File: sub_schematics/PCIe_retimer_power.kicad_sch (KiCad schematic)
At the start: 40 parts, among them U2 LMQ644A2QRXARQ1

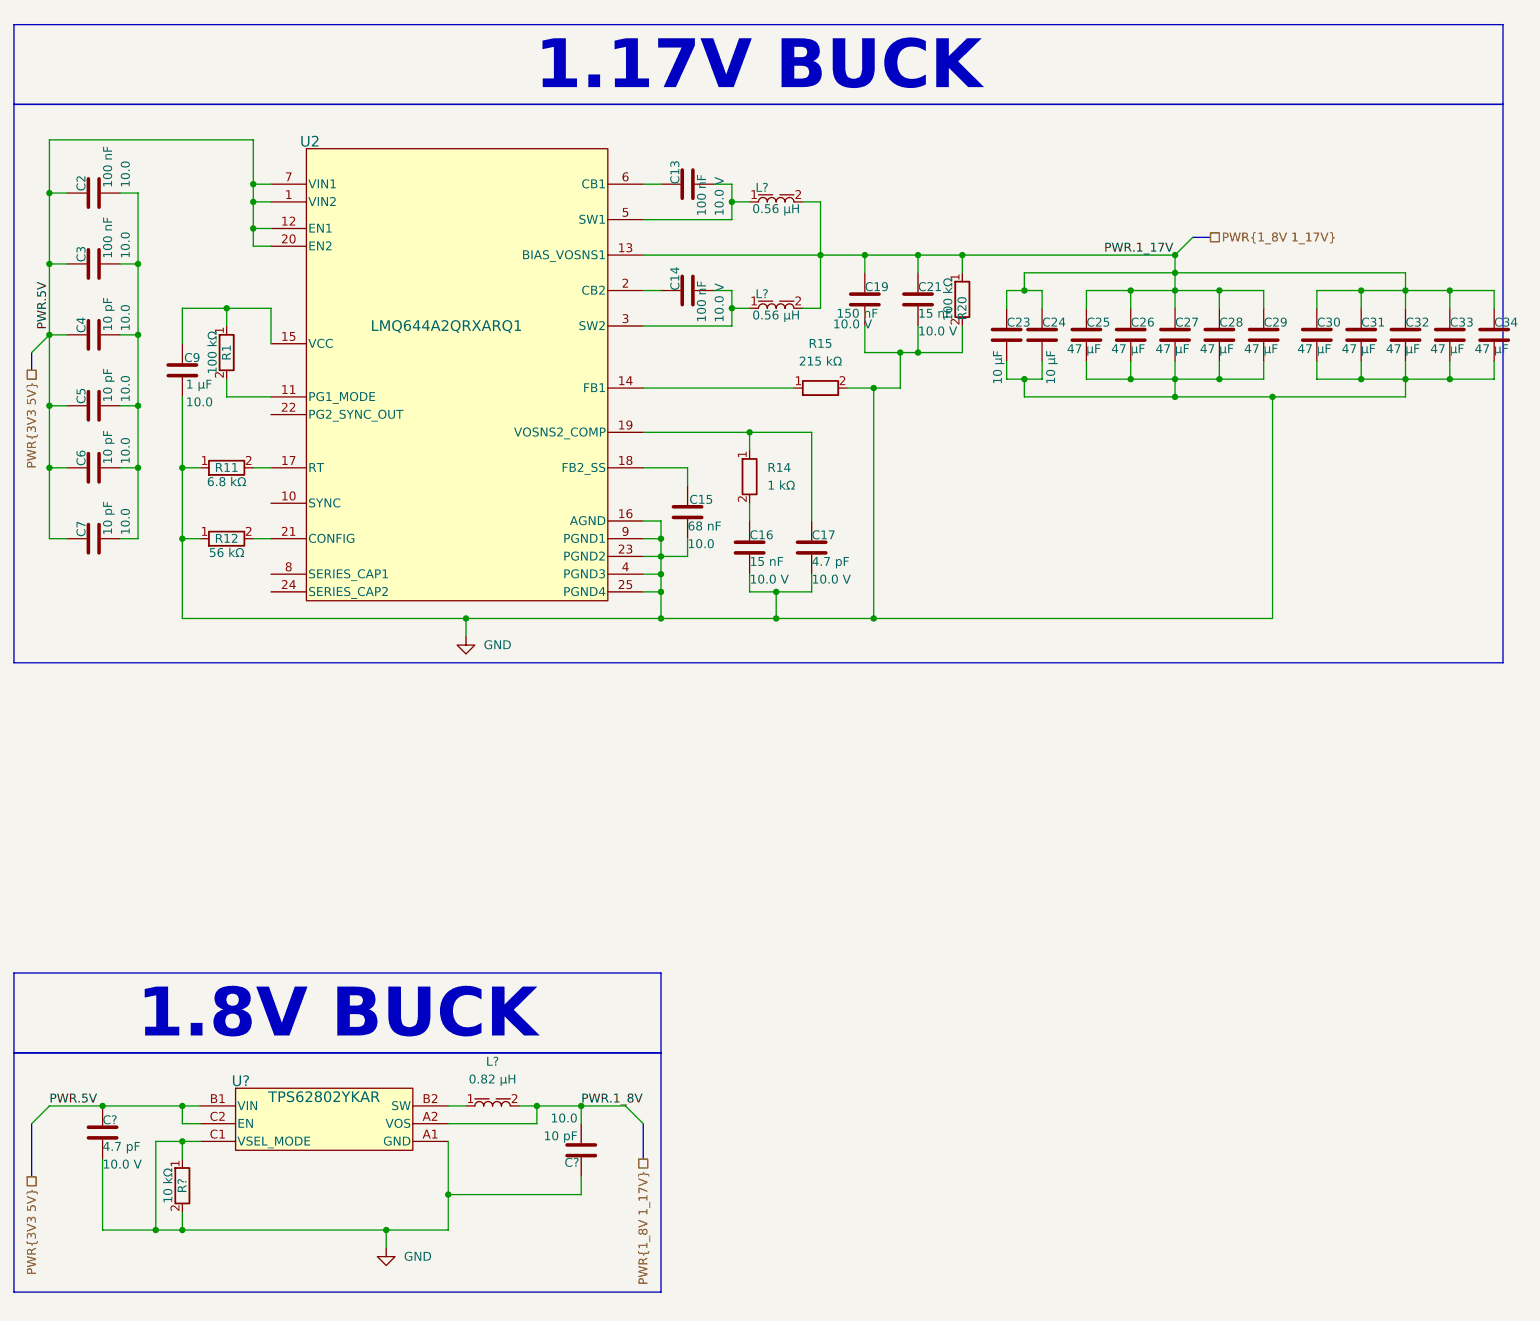
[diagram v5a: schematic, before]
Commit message: Buck closer to recommended value
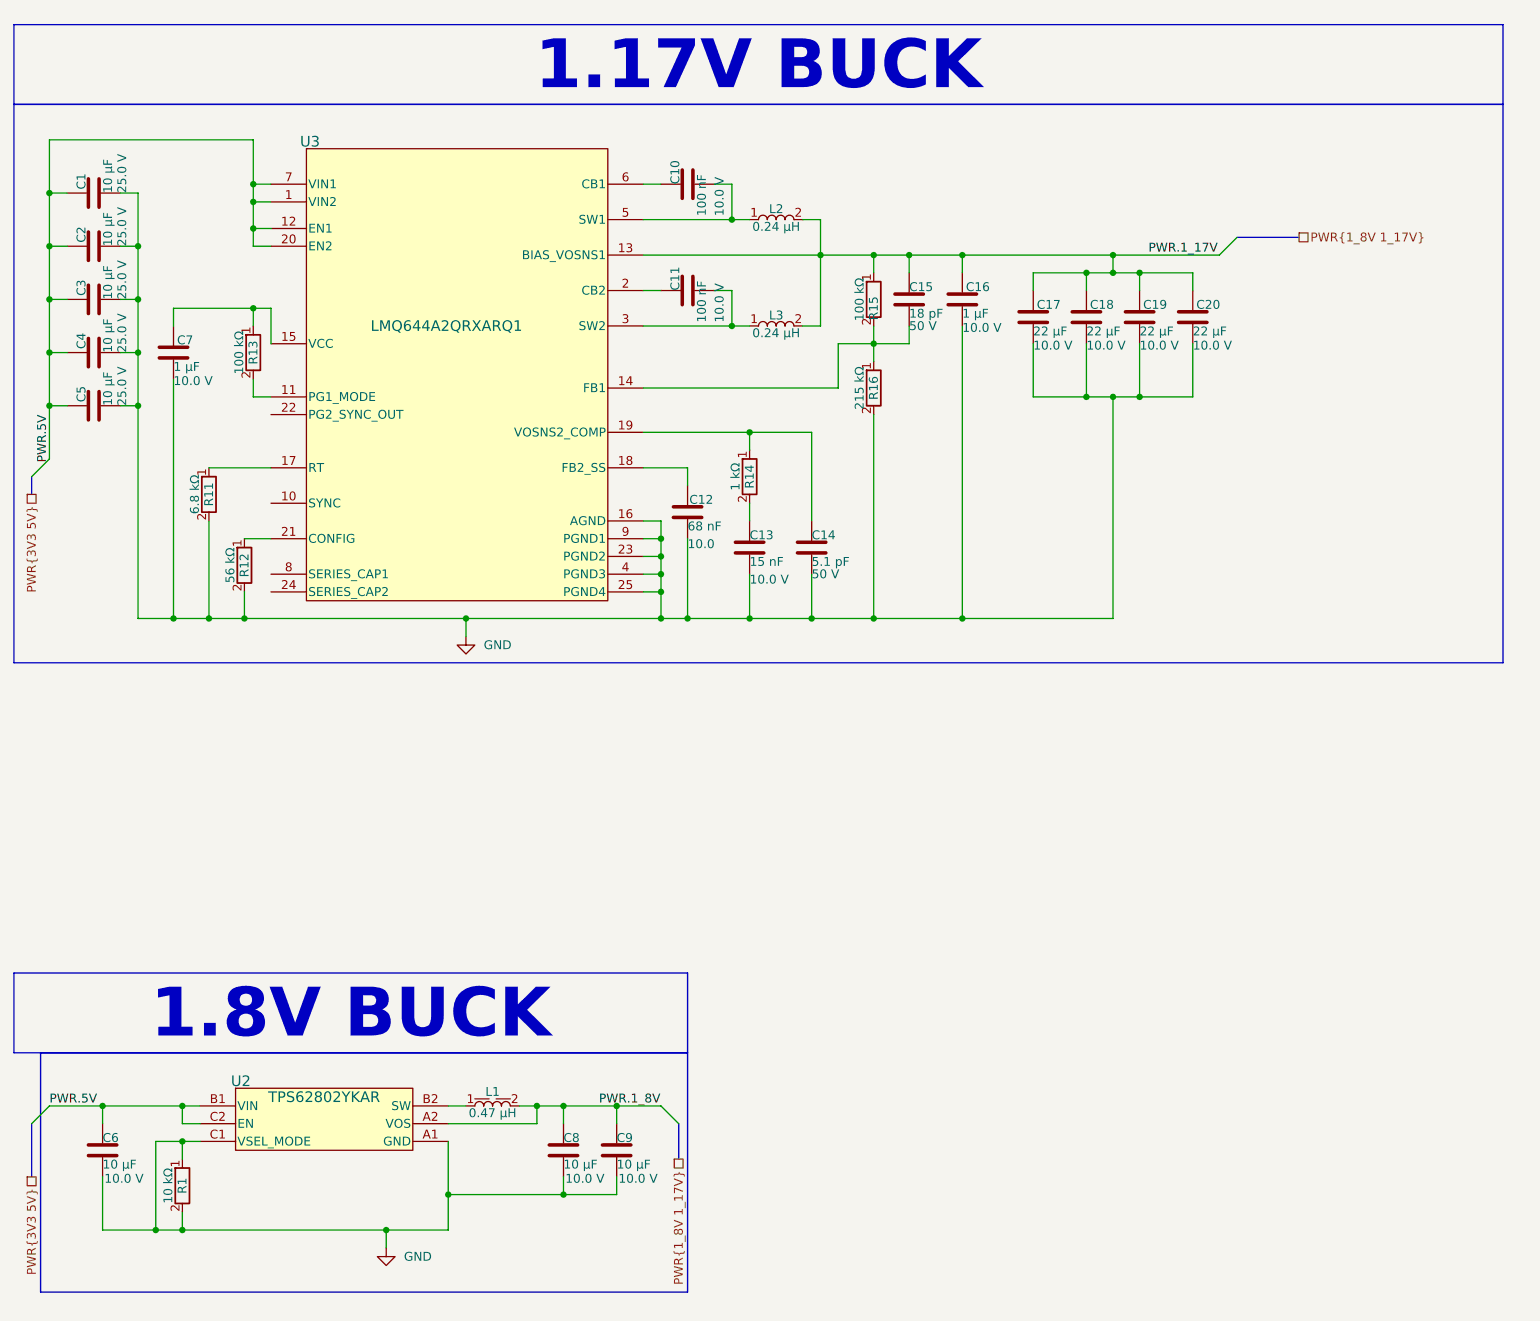
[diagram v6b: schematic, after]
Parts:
- removed C17, C?: 0603_R_885012006001, WE_WCAP-CSGP:C_Wurth_WCAP-CSGP-0603_R, symbol WE_WCAP-CSGP:0603_R_885012006001
- removed C19: 0603_R_885012206021, WE_WCAP-CSGP:C_Wurth_WCAP-CSGP-0603_R, symbol WE_WCAP-CSGP:0603_R_885012206021
- removed C2, C3: 0201_885012104002, WE_WCAP-CSGP:C_Wurth_WCAP-CSGP-0201, symbol WE_WCAP-CSGP:0201_885012104002
- removed C21: 0402_885012205013, WE_WCAP-CSGP:C_Wurth_WCAP-CSGP-0402, symbol WE_WCAP-CSGP:0402_885012205013
- removed C23, C24: 1210_H2.0_885012209005, WE_WCAP-CSGP:C_Wurth_WCAP-CSGP-1210_H2.0, symbol WE_WCAP-CSGP:1210_H2.0_885012209005
- removed C25, C26, C27, C28, C29, C30, C31, C32, C33, C34: 1206_H1.6_885012108012, WE_WCAP-CSGP:C_Wurth_WCAP-CSGP-1206_H1.6, symbol WE_WCAP-CSGP:1206_H1.6_885012108012
- removed C4, C5, C6, C7, C?: 1206_H0.8_885012008001, WE_WCAP-CSGP:C_Wurth_WCAP-CSGP-1206_H0.8, symbol WE_WCAP-CSGP:1206_H0.8_885012008001
- removed C9: 1210_H1.25_885012209003, WE_WCAP-CSGP:C_Wurth_WCAP-CSGP-1210_H1.25, symbol WE_WCAP-CSGP:1210_H1.25_885012209003
- removed L? (x2): 3012_744383340056, WE-MAPI:L_Wurth_WE-MAPI-3012, symbol WE-MAPI:3012_744383340056
- removed L?: 1610_744383130082, Inductor_SMD_Wurth:L_Wurth_WE-MAPI-1610, symbol WE-MAPI:1610_744383130082
- added C1, C2, C3, C4, C5: 0603_Fl0.35_R_885012106031, WE_WCAP-CSGP:C_Wurth_WCAP-CSGP-0603_Fl0.35_R, symbol WE_WCAP-CSGP:0603_Fl0.35_R_885012106031
- added C14: 0402_885392005058, WE_WCAP-CSRF:C_Wurth_WCAP-CSRF-0402, symbol WE_WCAP-CSRF:0402_885392005058
- added C15: 0402_885392005147, WE_WCAP-CSRF:C_Wurth_WCAP-CSRF-0402, symbol WE_WCAP-CSRF:0402_885392005147
- added C16, C7: 0402_885012105012, WE_WCAP-CSGP:C_Wurth_WCAP-CSGP-0402, symbol WE_WCAP-CSGP:0402_885012105012
- added C17, C18, C19, C20: 1206_H1.6_885012208019, WE_WCAP-CSGP:C_Wurth_WCAP-CSGP-1206_H1.6, symbol WE_WCAP-CSGP:1206_H1.6_885012208019
- added C6, C8, C9: 0402_885012105022, WE_WCAP-CSGP:C_Wurth_WCAP-CSGP-0402, symbol WE_WCAP-CSGP:0402_885012105022
- added L1: 2010_744383430047, WE-MAPI:L_Wurth_WE-MAPI-2010, symbol WE-WIND-MAPI:2010_744383430047
- added L2, L3: 201610_74479276124, WE-PMCI:L_Wurth_WE-PMCI-201610, symbol WE-WIND-PMC:201610_74479276124
- gave numbers to parts that had none: 2
- renumbered C13 to C10, C14 to C11, C15 to C12, C16 to C13, R1 to R13, R20 to R15, R15 to R16, U2 to U3
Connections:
- net GND: now also R11.2, R12.2, C1.2, C14.2, C16.2, C17.2, C18.2, C19.2, C2.2, C20.2, C3.2, C4.2, C5.2, C6.2, C7.2, C8.2, C9.2; no longer R11.1, R12.1, R15.2
- net PWR.1_17V: now also C15.1, C16.1, C17.1, C18.1, C19.1, C20.1, L2.2, L3.2
- net PWR.1_8V: now also C8.1, C9.1, L1.2
- net PWR.5V: now also C1.1, C2.1, C3.1, C4.1, C5.1, C6.1
- net at C10.2, U3.5 (SW1): now also L2.1
- net at R14.1, U3.19 (VOSNS2_COMP): now also C14.1
- net at C11.2, U3.3 (SW2): now also L3.1
- net at U3.21 (CONFIG): now also R12.1; no longer R12.2
- net at R16.1, U3.14 (FB1): now also R15.2, C15.2
- net at R13.1, U3.15 (VCC): now also C7.1
- net at U3.17 (RT): now also R11.1; no longer R11.2
- net at U2.B2 (SW): now also L1.1
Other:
- moved on the sheet: R11, R12, R13, R15, R16

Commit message: PCIe shematic fix
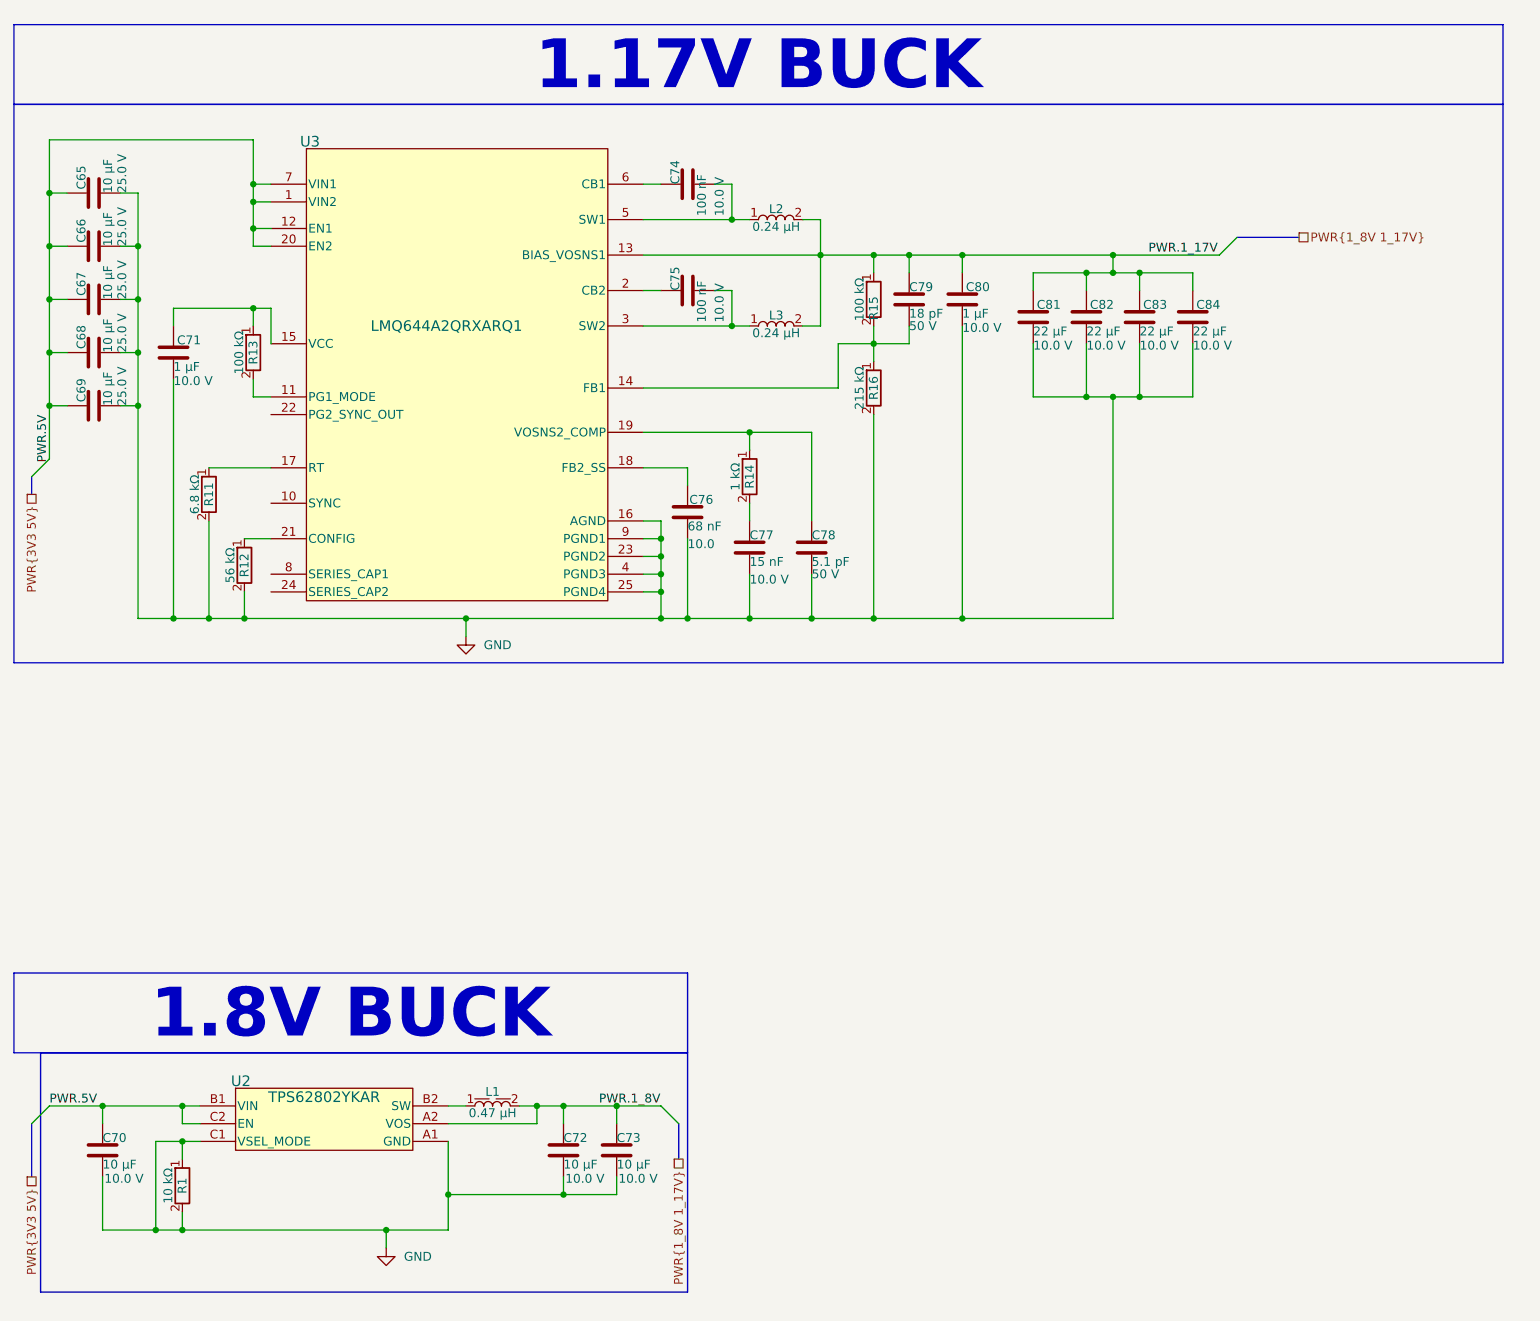
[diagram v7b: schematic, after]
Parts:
- renumbered C1 to C65, C2 to C66, C3 to C67, C4 to C68, C5 to C69, C6 to C70, C7 to C71, C8 to C72, C9 to C73, C10 to C74, C11 to C75, C12 to C76, C13 to C77, C14 to C78, C15 to C79, C16 to C80, C17 to C81, C18 to C82, C19 to C83, C20 to C84
